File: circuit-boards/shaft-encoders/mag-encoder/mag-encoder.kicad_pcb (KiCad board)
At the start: 4 copper layers, 26.7 x 31.8 mm, 20 parts, among them J1 0015912055, U1 AP2120N-3.3TRG1, U2 SN74LVC1G02DBVR, U3 MA732GQ

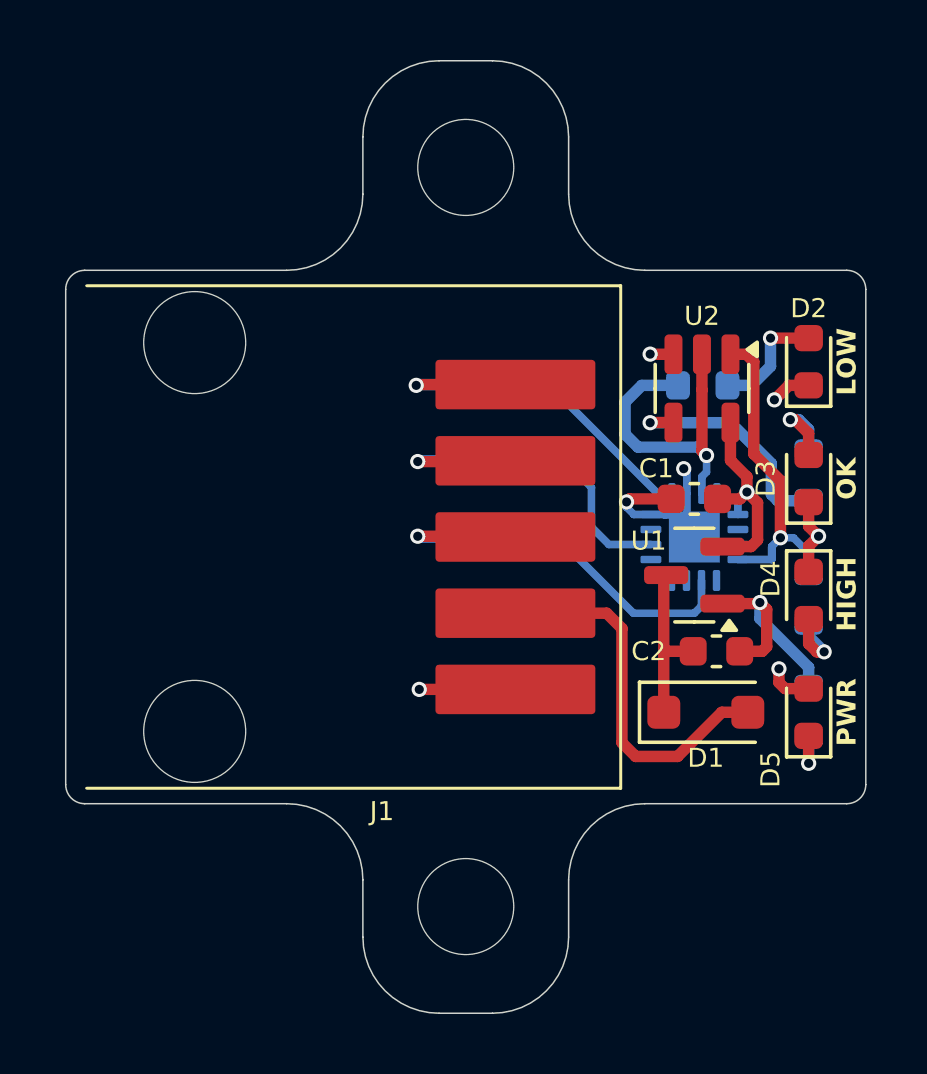
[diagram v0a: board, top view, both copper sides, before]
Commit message: Add SPI header for config. Center mounting holes on sensor
Signed-off-by: Scott <sgberman1@gmail.com>
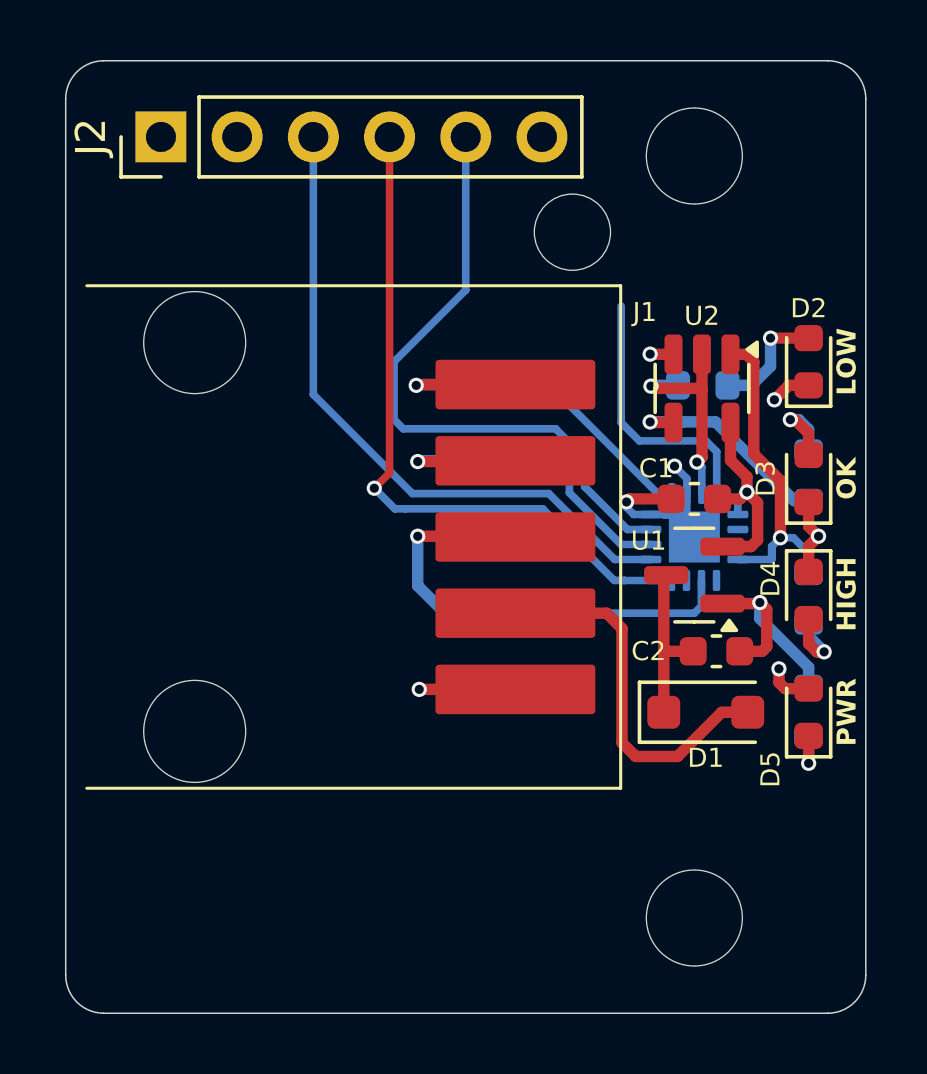
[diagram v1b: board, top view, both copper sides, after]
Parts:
- added H3: Pin, mag-encoder:pin-0.100, F.Cu at (224.5, 97.2)
- added H4: Slot, mag-encoder:slot-0.100x0.120, F.Cu at (224.5, 117.5)
- added J2: CONFIG, Connector_PinHeader_2.54mm:PinHeader_1x06_P2.54mm_Vertical, F.Cu at (210.8, 94.0)
- moved H1 7.63 mm to (228.6, 94.6)
- moved H2 7.63 mm to (228.6, 120.0)
- moved R7 2.54 mm to (222.2, 109.9)
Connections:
- U3 pad 12: unconnected-(U3-SCLK-Pad12) -> /SCLK
- U3 pad 4: unconnected-(U3-MOSI-Pad4) -> /MOSI
- U3 pad 5: unconnected-(U3-CS-Pad5) -> /CS
- U3 pad 7: unconnected-(U3-MISO-Pad7) -> /MISO
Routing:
- net /MOSI: track 0.00 -> 23.1 mm, vias 0 -> 1
- net /CS: track 0.00 -> 22.1 mm
- net /MISO: track 0.00 -> 21.1 mm
- net /SCLK: track 0.00 -> 8.87 mm
- net Net-(U3-MGL): track 10.8 -> 7.45 mm, vias 1 -> 2
- net /A: track 5.32 -> 7.38 mm
- net Net-(U3-A): track 7.77 -> 6.71 mm
- net Net-(R1-Pad1): track 7.74 -> 7.16 mm
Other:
- outline, holes or cut-outs redrawn
- board text added: "5-PWM 4-B 3-A 2-5V 1-GND"
